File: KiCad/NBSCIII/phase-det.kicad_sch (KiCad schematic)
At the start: 34 parts, among them Q1100 BC337-25, U1 LM324N

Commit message: unrescue Device:R_potentiometer
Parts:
- RV1100, RV1101: symbol NBSCIII-rescue:POT -> Device:R_Potentiometer
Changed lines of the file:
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@@
     (stroke (width 0) (type default) (color 0 0 0 0))
   )
-  (wire (pts (xy 262.89 35.56) (xy 262.89 40.64))
+  (wire (pts (xy 262.89 35.56) (xy 262.89 43.18))
     (stroke (width 0) (type default) (color 0 0 0 0))
   )
@@
     (stroke (width 0) (type default) (color 0 0 0 0))
   )
-  (wire (pts (xy 33.02 53.34) (xy 33.02 58.42))
+  (wire (pts (xy 33.02 50.8) (xy 33.02 58.42))
     (stroke (width 0) (type default) (color 0 0 0 0))
   )
@@
     (stroke (width 0) (type default) (color 0 0 0 0))
   )
-  (wire (pts (xy 33.02 36.83) (xy 33.02 40.64))
+  (wire (pts (xy 33.02 36.83) (xy 33.02 43.18))
     (stroke (width 0) (type default) (color 0 0 0 0))
   )
@@
     (stroke (width 0) (type default) (color 0 0 0 0))
   )
-  (wire (pts (xy 262.89 53.34) (xy 262.89 58.42))
+  (wire (pts (xy 262.89 50.8) (xy 262.89 58.42))
     (stroke (width 0) (type default) (color 0 0 0 0))
   )
@@
     (effects (font (size 1.524 1.524)) (justify right))
   )
-  (symbol (lib_id "NBSCIII-rescue:POT") (at 33.02 46.99 270) (unit 1)
-    (in_bom yes) (on_board yes)
-    (property "Reference" "RV1100" (id 0) (at 30.48 46.99 0))
-    (property "Value" "10k" (id 1) (at 33.02 46.99 0))
+  (symbol (lib_id "Device:R_Potentiometer") (at 33.02 46.99 0) (unit 1)
+    (in_bom yes) (on_board yes)
+    (property "Reference" "RV1100" (id 0) (at 26.67 50.8 0))
+    (property "Value" "10k" (id 1) (at 33.02 46.99 90))
     (property "Footprint" "" (id 2) (at 33.02 46.99 0)
       (effects (font (size 1.27 1.27)) hide)
@@
     (pin "2")
   )
-  (symbol (lib_id "NBSCIII-rescue:POT") (at 262.89 46.99 90) (unit 1)
-    (in_bom yes) (on_board yes)
-    (property "Reference" "RV1101" (id 0) (at 265.43 46.99 0))
-    (property "Value" "10k" (id 1) (at 262.89 46.99 0))
+  (symbol (lib_id "Device:R_Potentiometer") (at 262.89 46.99 180) (unit 1)
+    (in_bom yes) (on_board yes)
+    (property "Reference" "RV1101" (id 0) (at 269.24 48.26 0))
+    (property "Value" "10k" (id 1) (at 262.89 46.99 90))
     (property "Footprint" "" (id 2) (at 262.89 46.99 0)
       (effects (font (size 1.27 1.27)) hide)

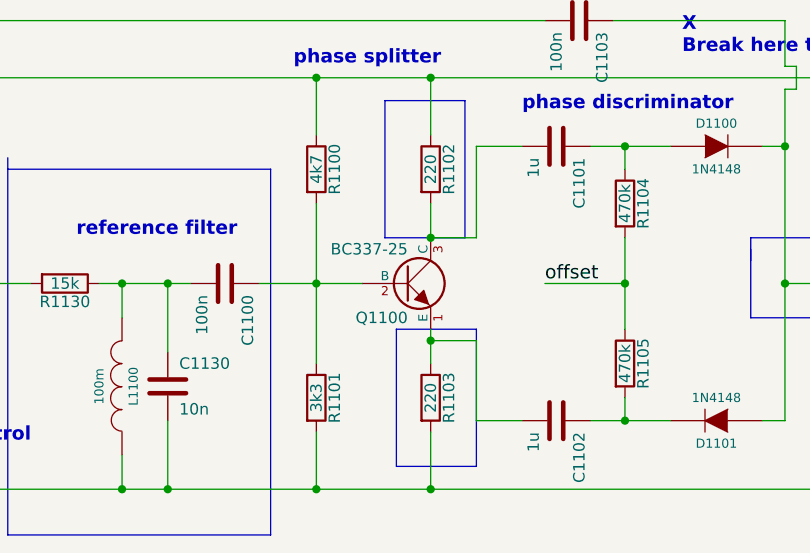
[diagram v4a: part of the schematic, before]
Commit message: unrescue NPN
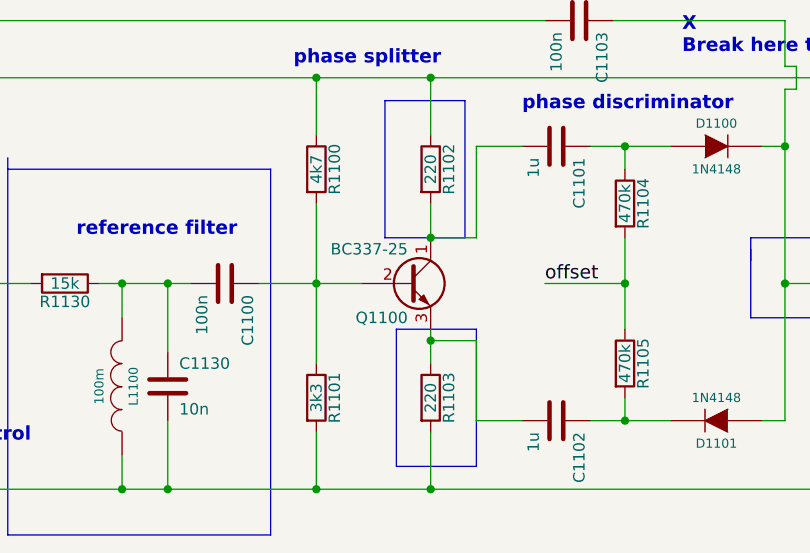
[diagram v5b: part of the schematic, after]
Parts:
- Q1100: symbol NBSCIII-rescue:NPN -> Device:Q_NPN_CBE
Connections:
- net at C1102.2, R1103.1: now also Q1100.3 (E); no longer Q1100.1 (E)
- net at C1101.2, R1102.2: now also Q1100.1 (C); no longer Q1100.3 (C)
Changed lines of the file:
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@@
     (pin "2")
   )
-  (symbol (lib_id "NBSCIII-rescue:NPN") (at 82.55 46.99 0) (unit 1)
+  (symbol (lib_id "Device:Q_NPN_CBE") (at 82.55 46.99 0) (unit 1)
     (in_bom yes) (on_board yes)
     (property "Reference" "Q1100" (id 0) (at 82.55 50.8 0)

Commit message: unrescue Device:D
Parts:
- D1100, D1101: symbol NBSCIII-rescue:DIODE -> Device:D
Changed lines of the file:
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@@
+    (stroke (width 0) (type default) (color 0 0 0 0))
+  )
+  (wire (pts (xy 106.68 62.23) (xy 113.03 62.23))
     (stroke (width 0) (type default) (color 0 0 0 0))
   )
@@
     (stroke (width 0) (type default) (color 0 0 0 0))
   )
-  (wire (pts (xy 106.68 31.75) (xy 111.76 31.75))
+  (wire (pts (xy 106.68 31.75) (xy 113.03 31.75))
     (stroke (width 0) (type default) (color 0 0 0 0))
   )
@@
     (stroke (width 0) (type default) (color 0 0 0 0))
   )
-  (wire (pts (xy 124.46 31.75) (xy 121.92 31.75))
+  (wire (pts (xy 120.65 31.75) (xy 124.46 31.75))
     (stroke (width 0) (type default) (color 0 0 0 0))
   )
@@
     (stroke (width 0) (type default) (color 0 0 0 0))
   )
-  (wire (pts (xy 121.92 62.23) (xy 124.46 62.23))
+  (wire (pts (xy 120.65 62.23) (xy 124.46 62.23))
     (stroke (width 0) (type default) (color 0 0 0 0))
   )
@@
   )
   (wire (pts (xy 151.13 24.13) (xy 179.07 24.13))
-    (stroke (width 0) (type default) (color 0 0 0 0))
-  )
-  (wire (pts (xy 106.68 62.23) (xy 111.76 62.23))
     (stroke (width 0) (type default) (color 0 0 0 0))
   )
@@
     (pin "2")
   )
-  (symbol (lib_id "NBSCIII-rescue:DIODE") (at 116.84 31.75 0) (unit 1)
+  (symbol (lib_id "Device:D") (at 116.84 31.75 0) (unit 1)
     (in_bom yes) (on_board yes)
     (property "Reference" "D1100" (id 0) (at 116.84 29.21 0)
@@
     (pin "2")
   )
-  (symbol (lib_id "NBSCIII-rescue:DIODE") (at 116.84 62.23 180) (unit 1)
+  (symbol (lib_id "Device:D") (at 116.84 62.23 180) (unit 1)
     (in_bom yes) (on_board yes)
     (property "Reference" "D1101" (id 0) (at 116.84 64.77 0)

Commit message: unrescue Device:L_small
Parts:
- L1100: symbol NBSCIII-rescue:INDUCTOR -> Device:L_Small
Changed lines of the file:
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@@
     (stroke (width 0) (type default) (color 0 0 0 0))
   )
-  (wire (pts (xy 50.8 66.04) (xy 50.8 69.85))
+  (wire (pts (xy 50.8 60.96) (xy 50.8 69.85))
     (stroke (width 0) (type default) (color 0 0 0 0))
   )
@@
     (stroke (width 0) (type default) (color 0 0 0 0))
   )
-  (wire (pts (xy 50.8 50.8) (xy 50.8 46.99))
+  (wire (pts (xy 50.8 46.99) (xy 50.8 55.88))
     (stroke (width 0) (type default) (color 0 0 0 0))
   )
@@
     (pin "3")
   )
-  (symbol (lib_id "NBSCIII-rescue:INDUCTOR") (at 50.8 58.42 180) (unit 1)
+  (symbol (lib_id "Device:L_Small") (at 50.8 58.42 180) (unit 1)
     (in_bom yes) (on_board yes)
     (property "Reference" "L1100" (id 0) (at 52.07 58.42 90)

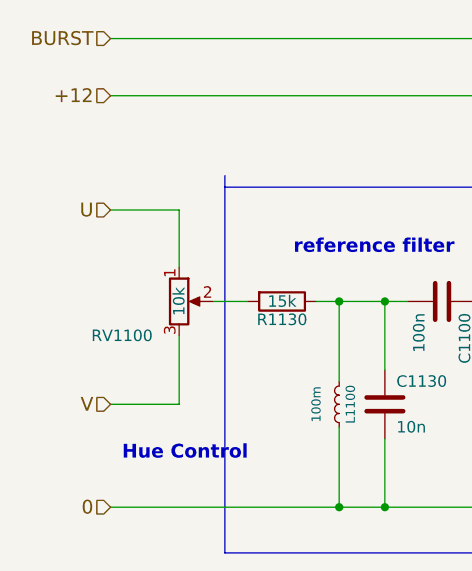
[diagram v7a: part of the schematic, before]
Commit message: Simplify power distribution and make global
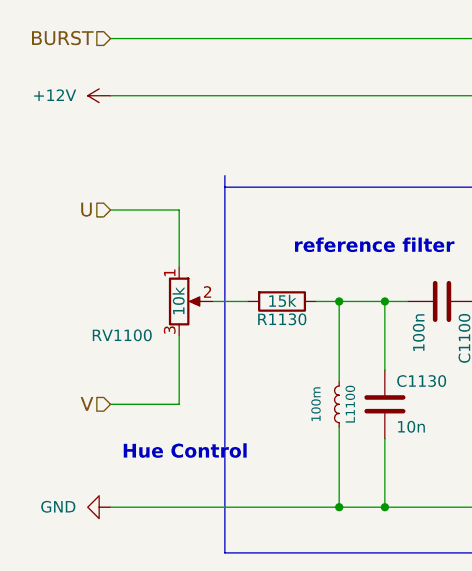
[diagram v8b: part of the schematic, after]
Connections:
- net +12 renamed +12V
- net 0 renamed GND
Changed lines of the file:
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@@
-    (effects (font (size 1.524 1.524)) (justify right))
-  )
-  (hierarchical_label "0" (shape input) (at 25.4 69.85 180)
-    (effects (font (size 1.524 1.524)) (justify right))
-  )
-  (hierarchical_label "+12" (shape input) (at 25.4 24.13 180)
     (effects (font (size 1.524 1.524)) (justify right))
   )
@@
     (pin "2")
   )
+  (symbol (lib_id "power:GND") (at 25.4 69.85 270) (unit 1)
+    (in_bom yes) (on_board yes) (fields_autoplaced)
+    (property "Reference" "#PWR0126" (id 0) (at 19.05 69.85 0)
+      (effects (font (size 1.27 1.27)) hide)
+    )
+    (property "Value" "GND" (id 1) (at 21.59 69.8499 90)
+      (effects (font (size 1.27 1.27)) (justify right))
+    )
+    (property "Footprint" "" (id 2) (at 25.4 69.85 0)
+      (effects (font (size 1.27 1.27)) hide)
+    )
+    (property "Datasheet" "" (id 3) (at 25.4 69.85 0)
+      (effects (font (size 1.27 1.27)) hide)
+    )
+    (pin "1")
+  )
+  (symbol (lib_id "power:+12V") (at 25.4 24.13 90) (unit 1)
+    (in_bom yes) (on_board yes) (fields_autoplaced)
+    (property "Reference" "#PWR0127" (id 0) (at 29.21 24.13 0)
+      (effects (font (size 1.27 1.27)) hide)
+    )
+    (property "Value" "+12V" (id 1) (at 21.59 24.1299 90)
+      (effects (font (size 1.27 1.27)) (justify left))
+    )
+    (property "Footprint" "" (id 2) (at 25.4 24.13 0)
+      (effects (font (size 1.27 1.27)) hide)
+    )
+    (property "Datasheet" "" (id 3) (at 25.4 24.13 0)
+      (effects (font (size 1.27 1.27)) hide)
+    )
+    (pin "1")
+  )
 )
